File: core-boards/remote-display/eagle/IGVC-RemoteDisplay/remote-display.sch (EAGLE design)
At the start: 32 parts, among them IC1 ATMEGA8, J1 B2PS-VH(LF)(SN), SW1 SPST_TACT-EVQQ2, T1 R-78E5.0-1.0, U1 ST7920, U2 MIC550X, X1 16MHz

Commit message: Redid component for LCD screen
And broke entire board
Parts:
- removed U$1: ROBOBUZZ1.0X, RoboJackets-Aesthetics:ROBOBUZZ1.0X
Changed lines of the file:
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@@
 <part name="R6" library="resistor" library_urn="urn:adsk.eagle:library:348" deviceset="R-US_" device="R0603" package3d_urn="urn:adsk.eagle:package:23555/2" value="470R"/>
 <part name="GND19" library="supply1" library_urn="urn:adsk.eagle:library:371" deviceset="GND" device=""/>
-<part name="U$1" library="RoboJackets-Aesthetics" deviceset="ROBOBUZZ" device="1.0X"/>
 </parts>
 <sheets>

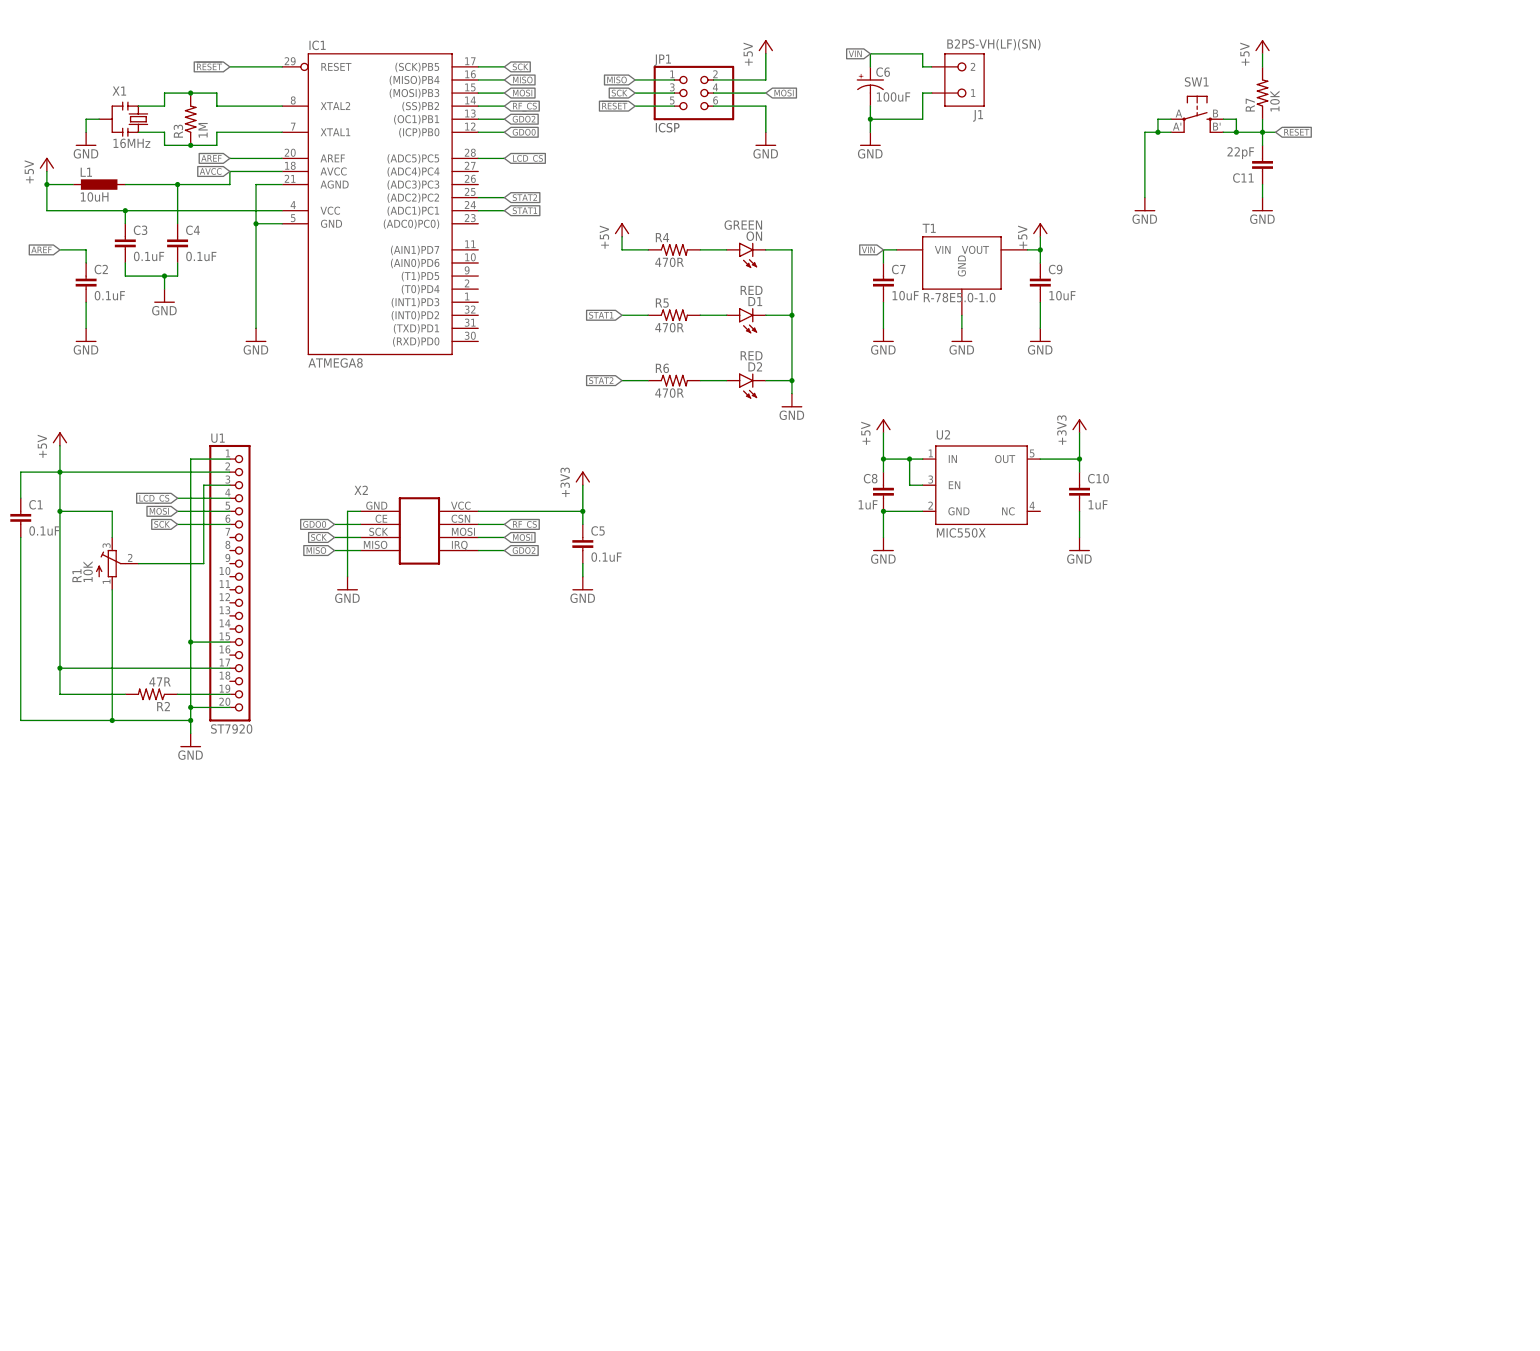
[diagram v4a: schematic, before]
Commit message: Reroute Remote Display Panel
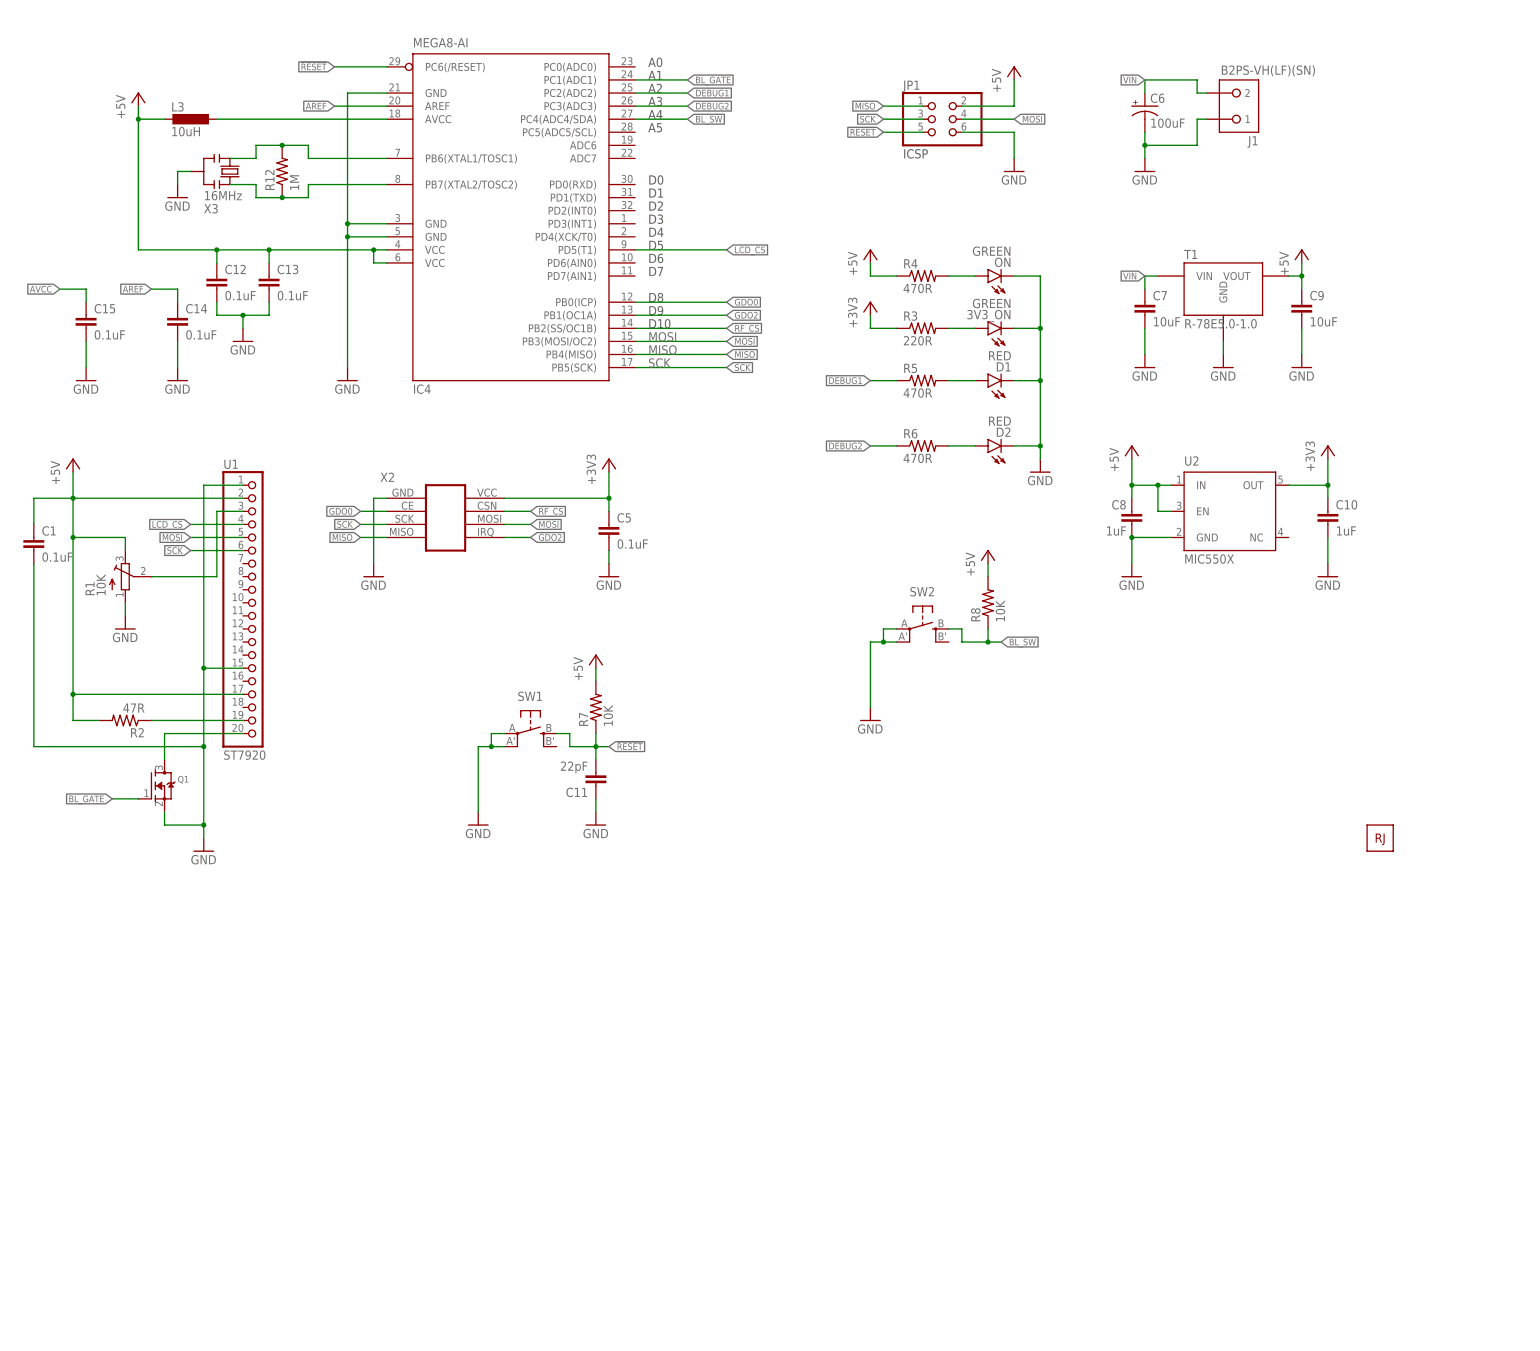
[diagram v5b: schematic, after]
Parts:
- removed C2, C3, C4: 0.1uF, resistor:C-EUC0603
- removed IC1: ATMEGA8, atmel:AT90S4433A
- removed L1: 10uH, IGVC-Remote:L-0805
- removed X1: 16MHz, IGVC-Remote:OSC_CSTCE16M0V53-R0
- added 3V3_ON: GREEN, led:LEDCHIP-LED0805
- added C12, C13, C14, C15: 0.1uF, resistor:C-EUC0603
- added IC4: MEGA8-AI, atmel:MEGA8-AI
- added L3: 10uH, IGVC-Remote:L-0805
- added Q1: (no value), adafruit:MOSFET-NREFLOW
- added R12: 1M, resistor:R-US_R0603
- added R8: 10K, resistor:R-US_R0603
- added SW2: SPST_TACT-EVQQ2, adafruit:SPST_TACT-EVQQ2
- added U$2: ROBOBUZZ1.0X, RoboJackets-Aesthetics:ROBOBUZZ1.0X
- added X3: 16MHz, IGVC-Remote:OSC_CSTCE16M0V53-R0
- R3: value 1M -> 220R
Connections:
- net N$3 renamed LCD_BL
- removed net STAT1: IC1.(ADC1)PC1, R5.1
- removed net STAT2: IC1.(ADC2)PC2, R6.1
- new net BL_DRAIN: Q1.D, U1.20
- new net BL_GATE: IC4.PC1(ADC1), Q1.G
- new net BL_SW: IC4.PC4(ADC4/SDA), R8.1, SW2.S
- new net DEBUG1: IC4.PC2(ADC2), R5.1
- new net DEBUG2: IC4.PC3(ADC3), R6.1
- new net PWR_LED1: 3V3_ON.A, R3.2
- net !RESET: now also IC4.PC6(/RESET); no longer IC1.RESET, SW1.S1
- net +3V3: now also R3.1
- net +5V: now also C12.1, C13.1, IC4.VCC@1, IC4.VCC@2, L3.2, R8.2; no longer C3.1, IC1.VCC, L1.2
- net AREF: now also C14.1, IC4.AREF; no longer C2.1, IC1.AREF
- net AVCC: now also C15.1, IC4.AVCC, L3.1; no longer C4.1, IC1.AVCC, L1.1
- net GDO0: now also IC4.PB0(ICP); no longer IC1.(ICP)PB0
- net GDO2: now also IC4.PB1(OC1A); no longer IC1.(OC1)PB1
- net GND: now also 3V3_ON.C, C12.2, C13.2, C14.2, C15.2, IC4.GND, IC4.GND@1, IC4.GND@2, Q1.S, SW2.P, SW2.P1, X3.2; no longer C2.2, C3.2, C4.2, IC1.AGND, IC1.GND, U1.20, X1.2
- net LCD_CS: now also IC4.PD5(T1); no longer IC1.(ADC5)PC5
- net MISO: now also IC4.PB4(MISO); no longer IC1.(MISO)PB4
- net MOSI: now also IC4.PB3(MOSI/OC2); no longer IC1.(MOSI)PB3
- net RF_CS: now also IC4.PB2(SS/OC1B); no longer IC1.(SS)PB2
- net SCK: now also IC4.PB5(SCK); no longer IC1.(SCK)PB5
- net XTAL1: now also IC4.PB6(XTAL1/TOSC1), R12.2, X3.1; no longer IC1.XTAL1, R3.1, X1.3
- net XTAL2: now also IC4.PB7(XTAL2/TOSC2), R12.1, X3.3; no longer IC1.XTAL2, R3.2, X1.1
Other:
- note added: "A0"
- note added: "A1"
- note added: "A2"
- note added: "A3"
- note added: "A4"
- note added: "A5"
- note added: "D0"
- note added: "D1"
- note added: "D10"
- note added: "D2"
- note added: "D3"
- note added: "D4"
- note added: "D5"
- note added: "D6"
- note added: "D7"
- note added: "D8"
- note added: "D9"
- moved on the sheet: C1, C10, C11, C5, C6, C7, C8, C9, D1, D2, J1, JP1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
